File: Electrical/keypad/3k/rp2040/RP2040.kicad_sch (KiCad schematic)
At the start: 85 parts, among them J1 Conn_01x04_Socket, J2 Conn_01x04_Socket, P1 USB-TYPE-C-016, Q1 BSS138, Q2 BSS138, SW1 KAN0644-0551B1-A, SW2 KAN0644-0551B1-A, SW3 KAN0644-0551B1-A, SW4 TS-1187A-B-A-B, SW5 TS-1187A-B-A-B, U1 ME6212C33M5G, U2 W25Q16JVSS, U3 PRTR5V0U2X, U4 RP2040, U5 SLSS49E, U6 SLSS49E, U7 SLSS49E, Y1 12MHz

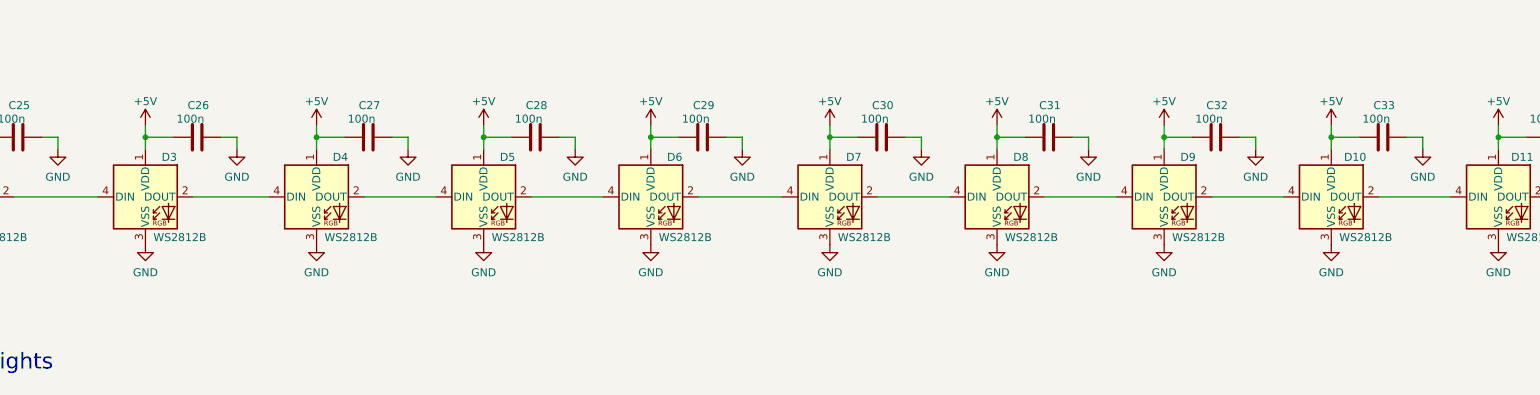
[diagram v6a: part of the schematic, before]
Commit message: adds 2020 led to smoothen out LED diffusing on sides
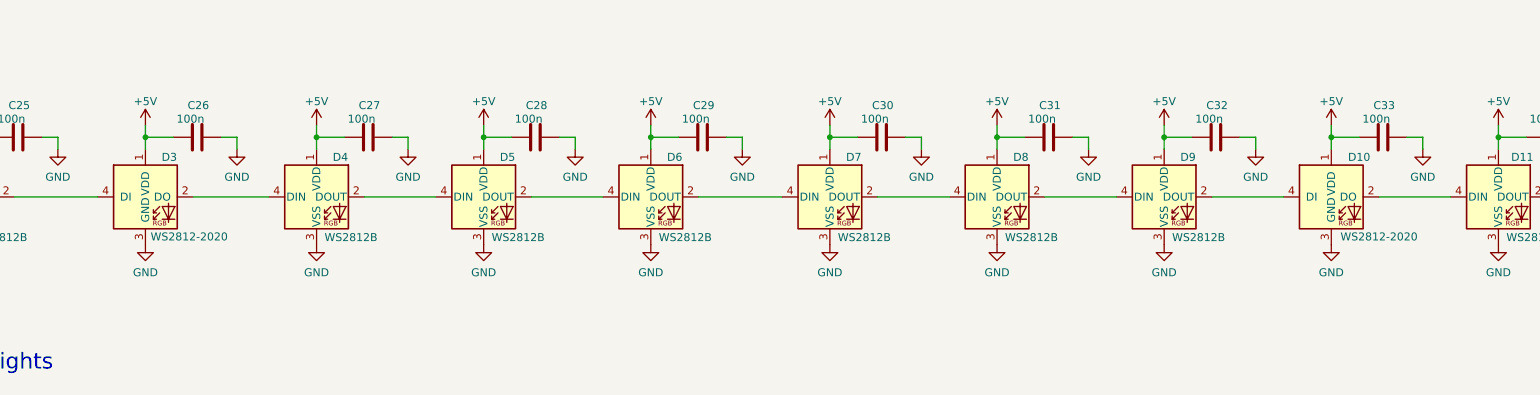
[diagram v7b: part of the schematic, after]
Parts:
- removed D10, D3: WS2812B, LED_SMD:LED_WS2812B_PLCC4_5.0x5.0mm_P3.2mm, symbol LED:WS2812B
- added D10, D3: WS2812-2020, footprints:LED_WS2812-2020, symbol WS2812-2020:WS2812-2020
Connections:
- net +5V: now also D10.1 (VDD), D3.1 (VDD)
- net GND: now also D10.3 (GND), D3.3 (GND)
- net at D4.4 (DIN): now also D3.2 (DO)
- net at D2.2 (DOUT): now also D3.4 (DI)
- net at D11.4 (DIN): now also D10.2 (DO)
- net at D9.2 (DOUT): now also D10.4 (DI)
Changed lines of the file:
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@@
+    )
+  )
+  (symbol (lib_id "WS2812-2020:WS2812-2020") (at 316.865 213.995 0) (unit 1)
+    (in_bom yes) (on_board yes) (dnp no)
+    (property "Reference" "D10" (at 321.31 207.645 0)
+      (effects (font (size 1.27 1.27)))
+    )
+    (property "Value" "WS2812-2020" (at 324.485 220.345 0)
+      (effects (font (size 1.27 1.27)))
+    )
+    (property "Footprint" "footprints:LED_WS2812-2020" (at 314.325 202.565 0)
+      (effects (font (size 1.27 1.27)) (justify bottom) hide)
+    )
+    (property "Datasheet" "" (at 316.865 213.995 0)
+      (effects (font (size 1.27 1.27)) hide)
+    )
+    (property "MF" "Worldsemi" (at 316.865 213.995 0)
+      (effects (font (size 1.27 1.27)) (justify bottom) hide)
+    )
+    (property "MAXIMUM_PACKAGE_HEIGHT" "0.84 mm" (at 316.865 213.995 0)
+      (effects (font (size 1.27 1.27)) (justify bottom) hide)
+    )
+    (property "Package" "Package" (at 313.055 205.105 0)
+      (effects (font (size 1.27 1.27)) (justify bottom) hide)
+    )
+    (property "Price" "None" (at 316.865 213.995 0)
+      (effects (font (size 1.27 1.27)) (justify bottom) hide)
+    )
+    (property "Check_prices" "https://www.snapeda.com/parts/WS2812-2020/Worldsemi/view-part/?ref=eda" (at 325.755 206.375 0)
+      (effects (font (size 1.27 1.27)) (justify bottom) hide)
+    )
+    (property "STANDARD" "Manufacturer Recommendations" (at 310.515 201.295 0)
+      (effects (font (size 1.27 1.27)) (justify bottom) hide)
+    )
+    (property "PARTREV" "V1.3" (at 316.865 213.995 0)
+      (effects (font (size 1.27 1.27)) (justify bottom) hide)
+    )
+    (property "SnapEDA_Link" "https://www.snapeda.com/parts/WS2812-2020/Worldsemi/view-part/?ref=snap" (at 314.325 203.835 0)
+      (effects (font (size 1.27 1.27)) (justify bottom) hide)
+    )
+    (property "MP" "WS2812-2020" (at 316.865 213.995 0)
+      (effects (font (size 1.27 1.27)) (justify bottom) hide)
+    )
+    (property "Description" "\nIntelligent control LED light source, SMD-4\n" (at 315.595 203.835 0)
+      (effects (font (size 1.27 1.27)) (justify bottom) hide)
+    )
+    (property "MANUFACTURER" "Worldsemi" (at 316.865 213.995 0)
+      (effects (font (size 1.27 1.27)) (justify bottom) hide)
+    )
+    (property "Availability" "Not in stock" (at 316.865 213.995 0)
+      (effects (font (size 1.27 1.27)) (justify bottom) hide)
+    )
+    (property "SNAPEDA_PN" "WS2812-2020" (at 316.865 213.995 0)
+      (effects (font (size 1.27 1.27)) (justify bottom) hide)
+    )
+    (pin "1")
+    (pin "2")
+    (pin "3")
+    (pin "4")
+    (instances
+      (project "RP2040"
+        (path "/26e500cb-9f3f-4e62-bb26-21a6be4a5bcc"
+          (reference "D10") (unit 1)
+        )
+      )
     )
   )
@@
     )
   )
-  (symbol (lib_id "LED:WS2812B") (at 127.635 213.995 0) (unit 1)
-    (in_bom yes) (on_board yes) (dnp no)
-    (property "Reference" "D3" (at 131.445 207.645 0)
-      (effects (font (size 1.27 1.27)))
-    )
-    (property "Value" "WS2812B" (at 128.905 219.71 0)
-      (effects (font (size 1.27 1.27)) (justify left top))
-    )
-    (property "Footprint" "LED_SMD:LED_WS2812B_PLCC4_5.0x5.0mm_P3.2mm" (at 128.905 221.615 0)
-      (effects (font (size 1.27 1.27)) (justify left top) hide)
-    )
-    (property "Datasheet" "https://cdn-shop.adafruit.com/datasheets/WS2812B.pdf" (at 130.175 223.52 0)
-      (effects (font (size 1.27 1.27)) (justify left top) hide)
-    )
-    (pin "1")
-    (pin "2")
-    (pin "3")
-    (pin "4")
-    (instances
-      (project "RP2040"
-        (path "/26e500cb-9f3f-4e62-bb26-21a6be4a5bcc"
-          (reference "D3") (unit 1)
-        )
-      )
-    )
-  )
   (symbol (lib_id "power:+5V") (at 290.195 202.565 0) (unit 1)
     (in_bom yes) (on_board yes) (dnp no)
@@
   )
   (symbol (lib_name "GND_1") (lib_id "power:GND") (at 142.24 206.375 0) (unit 1)
-    (in_bom yes) (on_board yes) (dnp no) (fields_autoplaced)
+    (in_bom yes) (on_board yes) (dnp no)
     (property "Reference" "#PWR060" (at 142.24 212.725 0)
       (effects (font (size 1.27 1.27)) hide)
@@
     )
   )
-  (symbol (lib_id "LED:WS2812B") (at 316.865 213.995 0) (unit 1)
-    (in_bom yes) (on_board yes) (dnp no)
-    (property "Reference" "D10" (at 320.675 207.645 0)
-      (effects (font (size 1.27 1.27)))
-    )
-    (property "Value" "WS2812B" (at 318.135 219.71 0)
-      (effects (font (size 1.27 1.27)) (justify left top))
-    )
-    (property "Footprint" "LED_SMD:LED_WS2812B_PLCC4_5.0x5.0mm_P3.2mm" (at 318.135 221.615 0)
-      (effects (font (size 1.27 1.27)) (justify left top) hide)
-    )
-    (property "Datasheet" "https://cdn-shop.adafruit.com/datasheets/WS2812B.pdf" (at 319.405 223.52 0)
-      (effects (font (size 1.27 1.27)) (justify left top) hide)
-    )
-    (pin "1")
-    (pin "2")
-    (pin "3")
-    (pin "4")
-    (instances
-      (project "RP2040"
-        (path "/26e500cb-9f3f-4e62-bb26-21a6be4a5bcc"
-          (reference "D10") (unit 1)
-        )
-      )
-    )
-  )
   (symbol (lib_id "power:+5V") (at 59.055 201.295 0) (unit 1)
     (in_bom yes) (on_board yes) (dnp no)
@@
         )
       )
+    )
+  )
+  (symbol (lib_id "WS2812-2020:WS2812-2020") (at 127.635 213.995 0) (unit 1)
+    (in_bom yes) (on_board yes) (dnp no)
+    (property "Reference" "D3" (at 131.445 207.645 0)
+      (effects (font (size 1.27 1.27)))
+    )
+    (property "Value" "WS2812-2020" (at 134.62 220.345 0)
+      (effects (font (size 1.27 1.27)))
+    )
+    (property "Footprint" "footprints:LED_WS2812-2020" (at 125.095 202.565 0)
+      (effects (font (size 1.27 1.27)) (justify bottom) hide)
+    )
+    (property "Datasheet" "" (at 127.635 213.995 0)
+      (effects (font (size 1.27 1.27)) hide)
+    )
+    (property "MF" "Worldsemi" (at 127.635 213.995 0)
+      (effects (font (size 1.27 1.27)) (justify bottom) hide)
+    )
+    (property "MAXIMUM_PACKAGE_HEIGHT" "0.84 mm" (at 127.635 213.995 0)
+      (effects (font (size 1.27 1.27)) (justify bottom) hide)
+    )
+    (property "Package" "Package" (at 123.825 205.105 0)
+      (effects (font (size 1.27 1.27)) (justify bottom) hide)
+    )
+    (property "Price" "None" (at 127.635 213.995 0)
+      (effects (font (size 1.27 1.27)) (justify bottom) hide)
+    )
+    (property "Check_prices" "https://www.snapeda.com/parts/WS2812-2020/Worldsemi/view-part/?ref=eda" (at 136.525 206.375 0)
+      (effects (font (size 1.27 1.27)) (justify bottom) hide)
+    )
+    (property "STANDARD" "Manufacturer Recommendations" (at 121.285 201.295 0)
+      (effects (font (size 1.27 1.27)) (justify bottom) hide)
+    )
+    (property "PARTREV" "V1.3" (at 127.635 213.995 0)
+      (effects (font (size 1.27 1.27)) (justify bottom) hide)
+    )
+    (property "SnapEDA_Link" "https://www.snapeda.com/parts/WS2812-2020/Worldsemi/view-part/?ref=snap" (at 125.095 203.835 0)
+      (effects (font (size 1.27 1.27)) (justify bottom) hide)
+    )
+    (property "MP" "WS2812-2020" (at 127.635 213.995 0)
+      (effects (font (size 1.27 1.27)) (justify bottom) hide)
+    )
+    (property "Description" "\nIntelligent control LED light source, SMD-4\n" (at 126.365 203.835 0)
+      (effects (font (size 1.27 1.27)) (justify bottom) hide)
+    )
+    (property "MANUFACTURER" "Worldsemi" (at 127.635 213.995 0)
+      (effects (font (size 1.27 1.27)) (justify bottom) hide)
+    )
+    (property "Availability" "Not in stock" (at 127.635 213.995 0)
+      (effects (font (size 1.27 1.27)) (justify bottom) hide)
+    )
+    (property "SNAPEDA_PN" "WS2812-2020" (at 127.635 213.995 0)
+      (effects (font (size 1.27 1.27)) (justify bottom) hide)
+    )
+    (pin "1")
+    (pin "2")
+    (pin "3")
+    (pin "4")
+    (instances
+      (project "RP2040"
+        (path "/26e500cb-9f3f-4e62-bb26-21a6be4a5bcc"
+          (reference "D3") (unit 1)
+        )
+      )

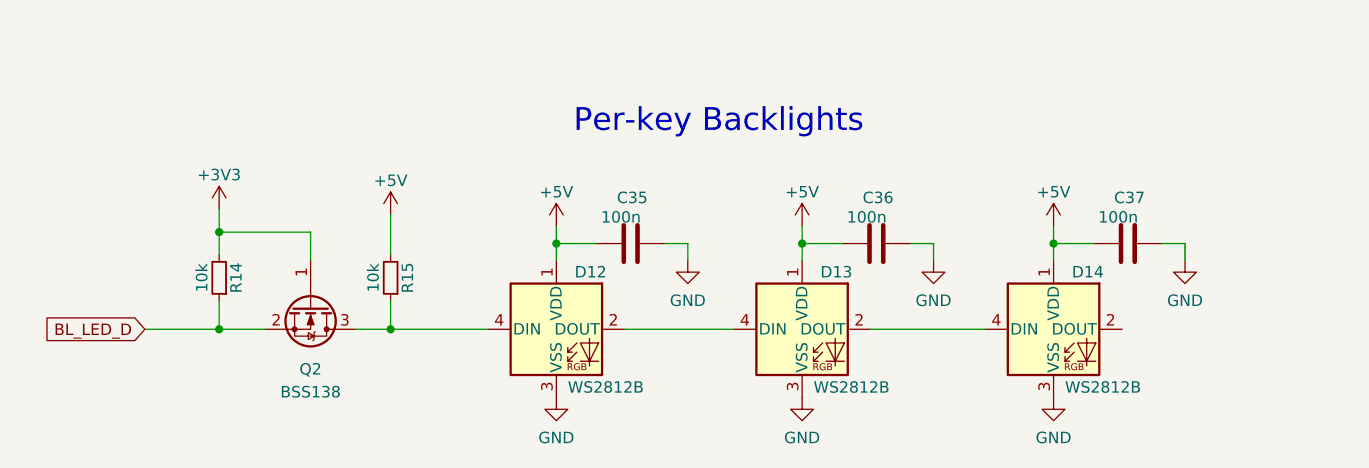
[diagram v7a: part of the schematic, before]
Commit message: changes led per-key backlights to 2020 and adds more screw holes for tilting issue
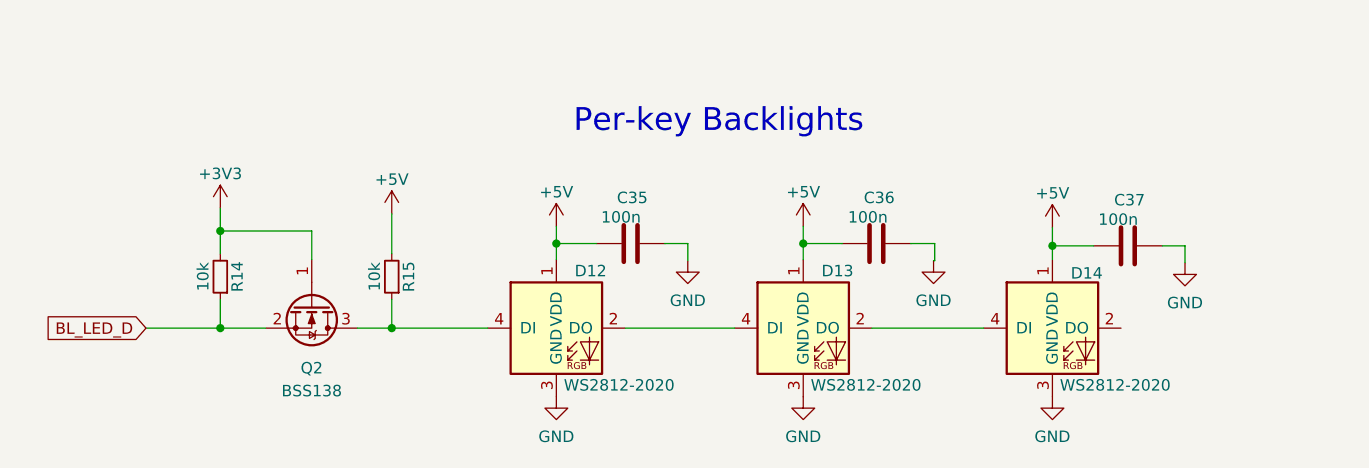
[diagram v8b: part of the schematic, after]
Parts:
- removed D12, D13, D14: WS2812B, LED_SMD:LED_WS2812B_PLCC4_5.0x5.0mm_P3.2mm, symbol LED:WS2812B
- added D12, D13, D14: WS2812-2020, footprints:LED_WS2812-2020, symbol WS2812-2020:WS2812-2020
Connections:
- net +5V: now also D12.1 (VDD), D13.1 (VDD), D14.1 (VDD)
- net GND: now also D12.3 (GND), D13.3 (GND), D14.3 (GND)
- net at Q2.3 (D), R15.1: now also D12.4 (DI)
- new net: D12.2 (DO), D13.4 (DI)
- new net: D13.2 (DO), D14.4 (DI)
